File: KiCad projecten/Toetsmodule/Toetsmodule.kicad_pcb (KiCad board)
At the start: 2 copper layers, 50 x 50 mm, 8 parts, among them J1 Conn_01x03_Male, J2 Touch module, J3 Conn_01x06_Male, J4 Conn_01x03_Male

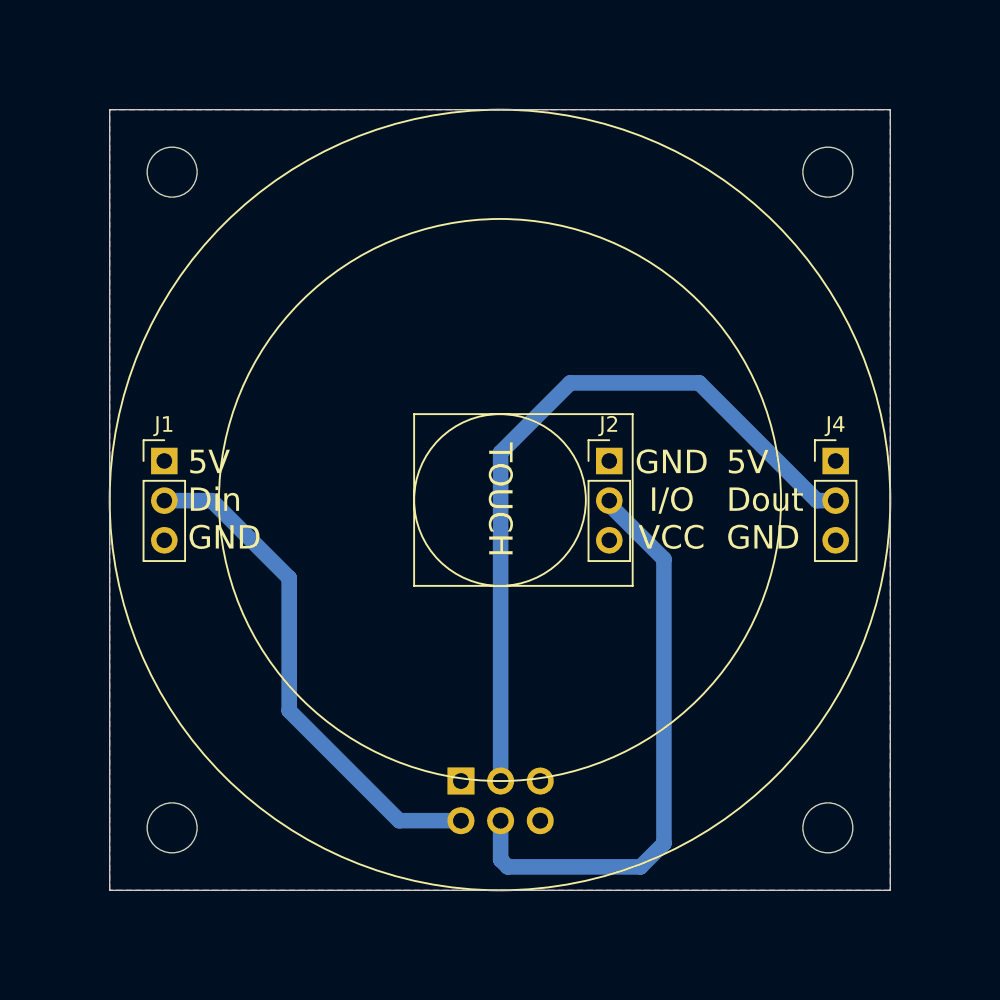
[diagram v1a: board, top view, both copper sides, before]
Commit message: Update toetsmodule: 60 x 60 mm & M4 gaten
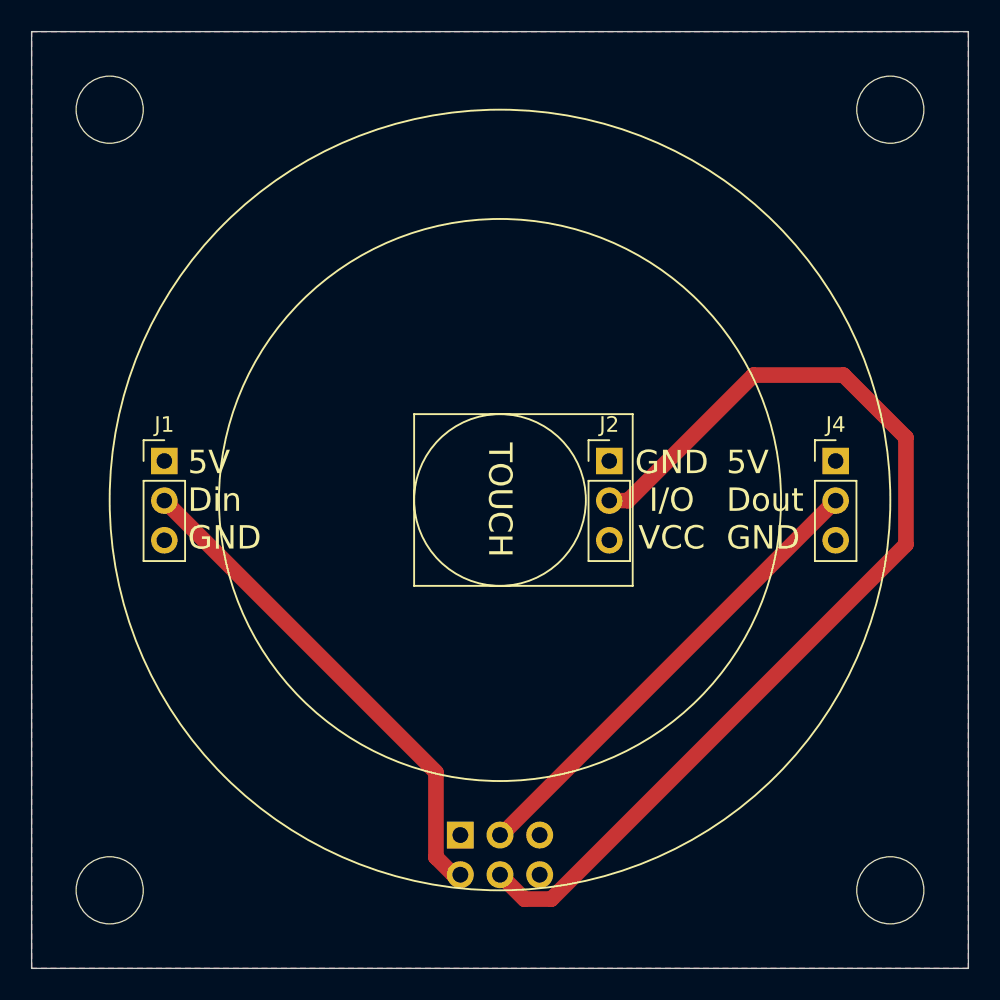
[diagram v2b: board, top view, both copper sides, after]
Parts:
- removed the REF** at (104.0, 136.0)
- removed the REF** at (146.0, 136.0)
- removed the REF** at (104.0, 94.0)
- removed the REF** at (146.0, 94.0)
- added REF**: MountingHole_4.3mm_M4, Mounting_Holes:MountingHole_4.3mm_M4, F.Cu at (150.0, 140.0)
- added REF**: MountingHole_4.3mm_M4, Mounting_Holes:MountingHole_4.3mm_M4, F.Cu at (100.0, 140.0)
- added REF**: MountingHole_4.3mm_M4, Mounting_Holes:MountingHole_4.3mm_M4, F.Cu at (100.0, 90.0)
- added REF**: MountingHole_4.3mm_M4, Mounting_Holes:MountingHole_4.3mm_M4, F.Cu at (150.0, 90.0)
- moved J3 3.46 mm to (122.5, 136.5)
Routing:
- net /Touch_output: track 37.2 -> 66.9 mm
- net /LED_out: track 47.5 -> 30.4 mm
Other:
- board size 50 x 50 mm -> 60 x 60 mm
